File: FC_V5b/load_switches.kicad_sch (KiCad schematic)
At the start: 39 parts, among them U19 AP22652, U21 AP22652, U22 AP22652, U23 AP22652, U24 AP22652, U25 TPS2HB50AQPWPRQ1, U29 AP22652, U6 TPS4H160AQPWPRQ1

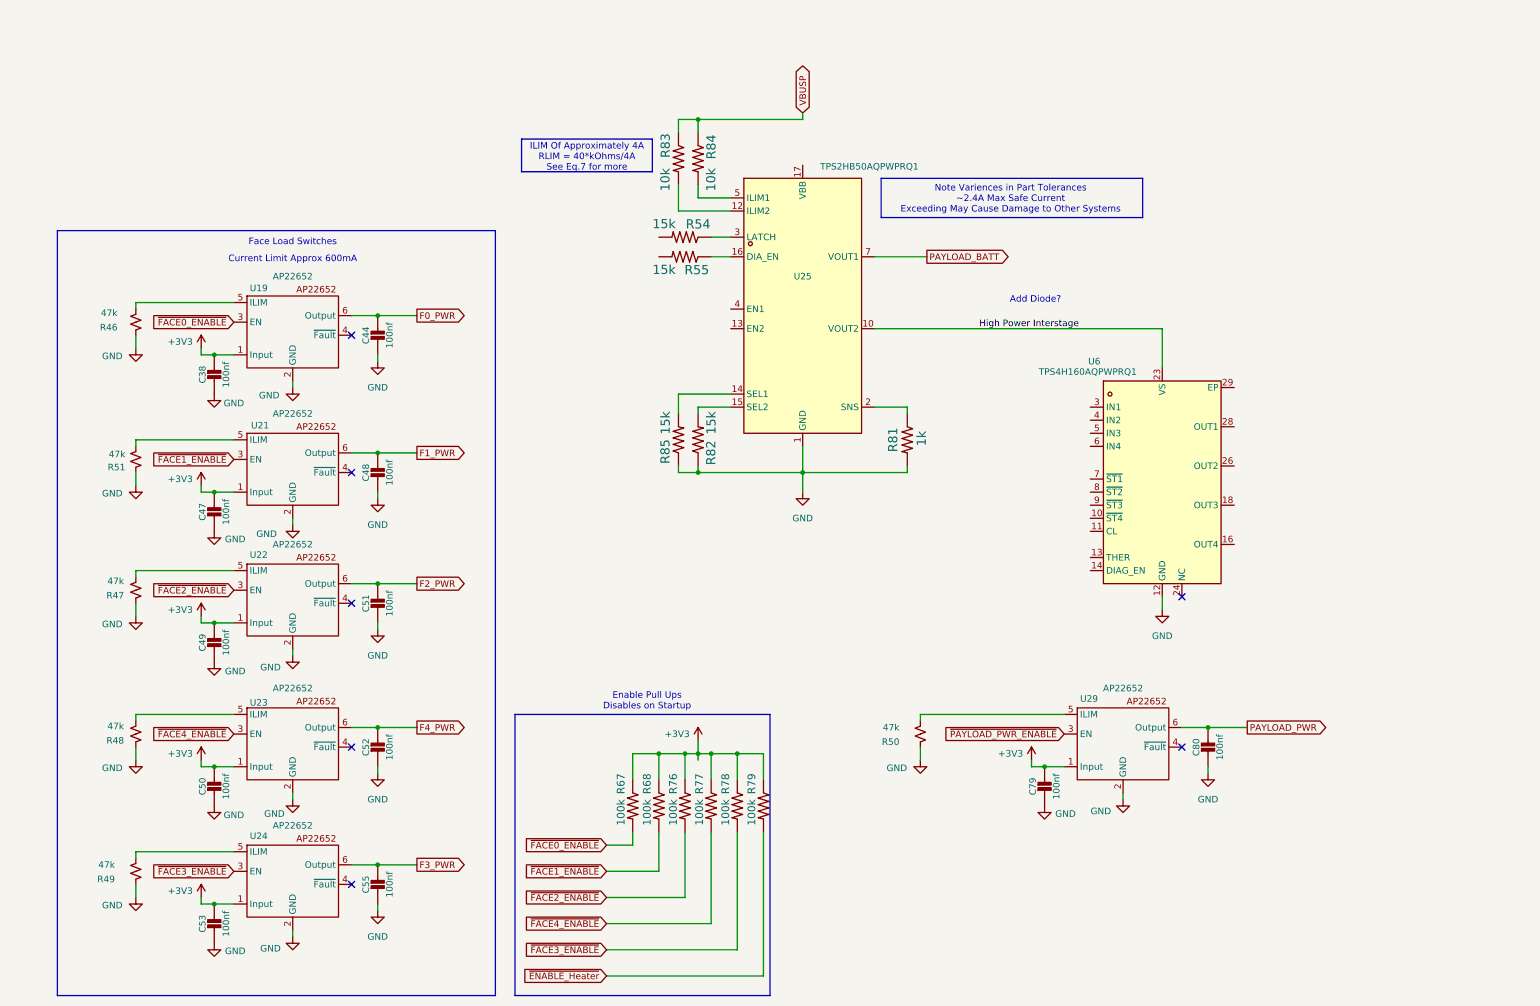
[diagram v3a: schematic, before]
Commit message: Added TPS2 and TPS4 Load Switch Schematics
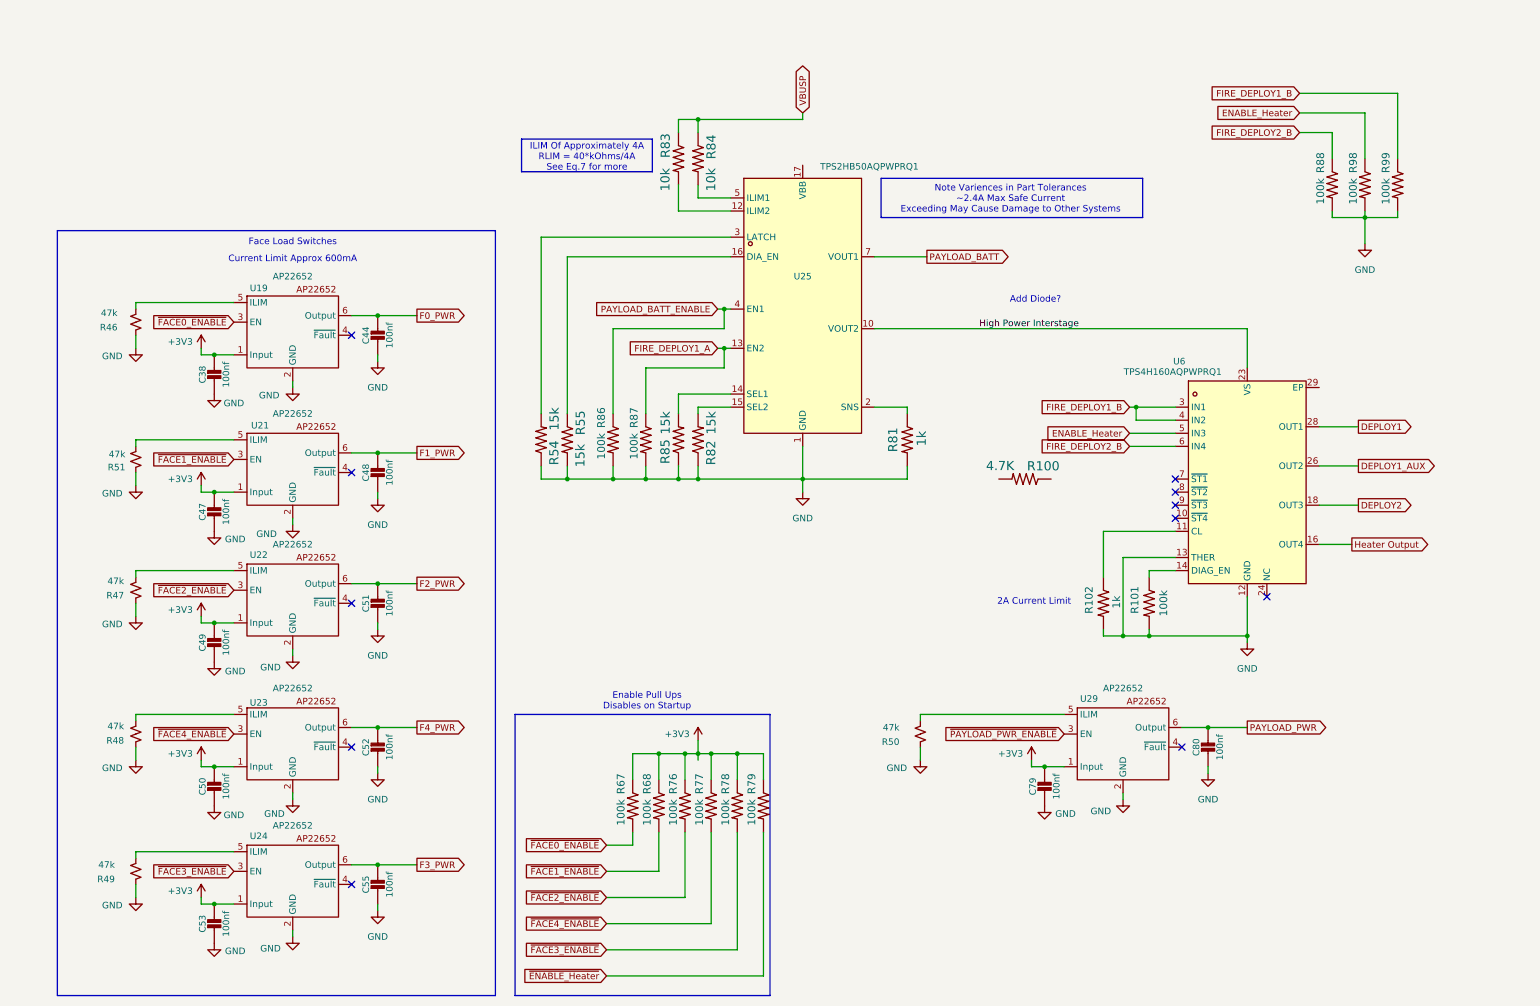
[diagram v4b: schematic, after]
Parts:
- added R100: 4.7K, Resistor_SMD:R_0603_1608Metric, symbol mainboard:RESISTOR0603
- added R101, R86, R87, R88, R98, R99: 100k, Resistor_SMD:R_0603_1608Metric, symbol mainboard:R-US_R0603
- added R102: 1k, Resistor_SMD:R_0603_1608Metric, symbol mainboard:R-US_R0603
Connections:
- net GND: now also R54.1, R55.2, U6.13 (THER), R101.2, R102.2, R86.2, R87.2, R88.2, R98.2, R99.2
- net at U25.3 (LATCH): now also R54.2; no longer R54.1
- net FIRE_DEPLOY1_A: now reaches U25.13 (EN2)
- net FIRE_DEPLOY1_A: now also R87.1
- net PAYLOAD_BATT_ENABLE: now reaches U25.4 (EN1)
- net PAYLOAD_BATT_ENABLE: now also R86.1
- net at U6.11 (CL): now also R102.1
- net at U6.14 (DIAG_EN): now also R101.1
- net Heater Output: now reaches U6.15 (OUT4), U6.16 (OUT4)
- net DEPLOY2: now reaches U6.17 (OUT3), U6.18 (OUT3)
- net DEPLOY1_AUX: now reaches U6.25 (OUT2), U6.26 (OUT2)
- net DEPLOY1: now reaches U6.27 (OUT1), U6.28 (OUT1)
- net FIRE_DEPLOY1_B: now reaches U6.3 (IN1)
- net FIRE_DEPLOY1_B: now also U6.4 (IN2), R99.1
- net ENABLE_Heater: now reaches U6.5 (IN3)
- net ENABLE_Heater: now also R98.1
- net FIRE_DEPLOY2_B: now reaches U6.6 (IN4)
- net FIRE_DEPLOY2_B: now also R88.1
- no-connect marks 7 -> 11
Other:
- note added: "2A Current Limit"
- moved on the sheet: R54, R55, U6

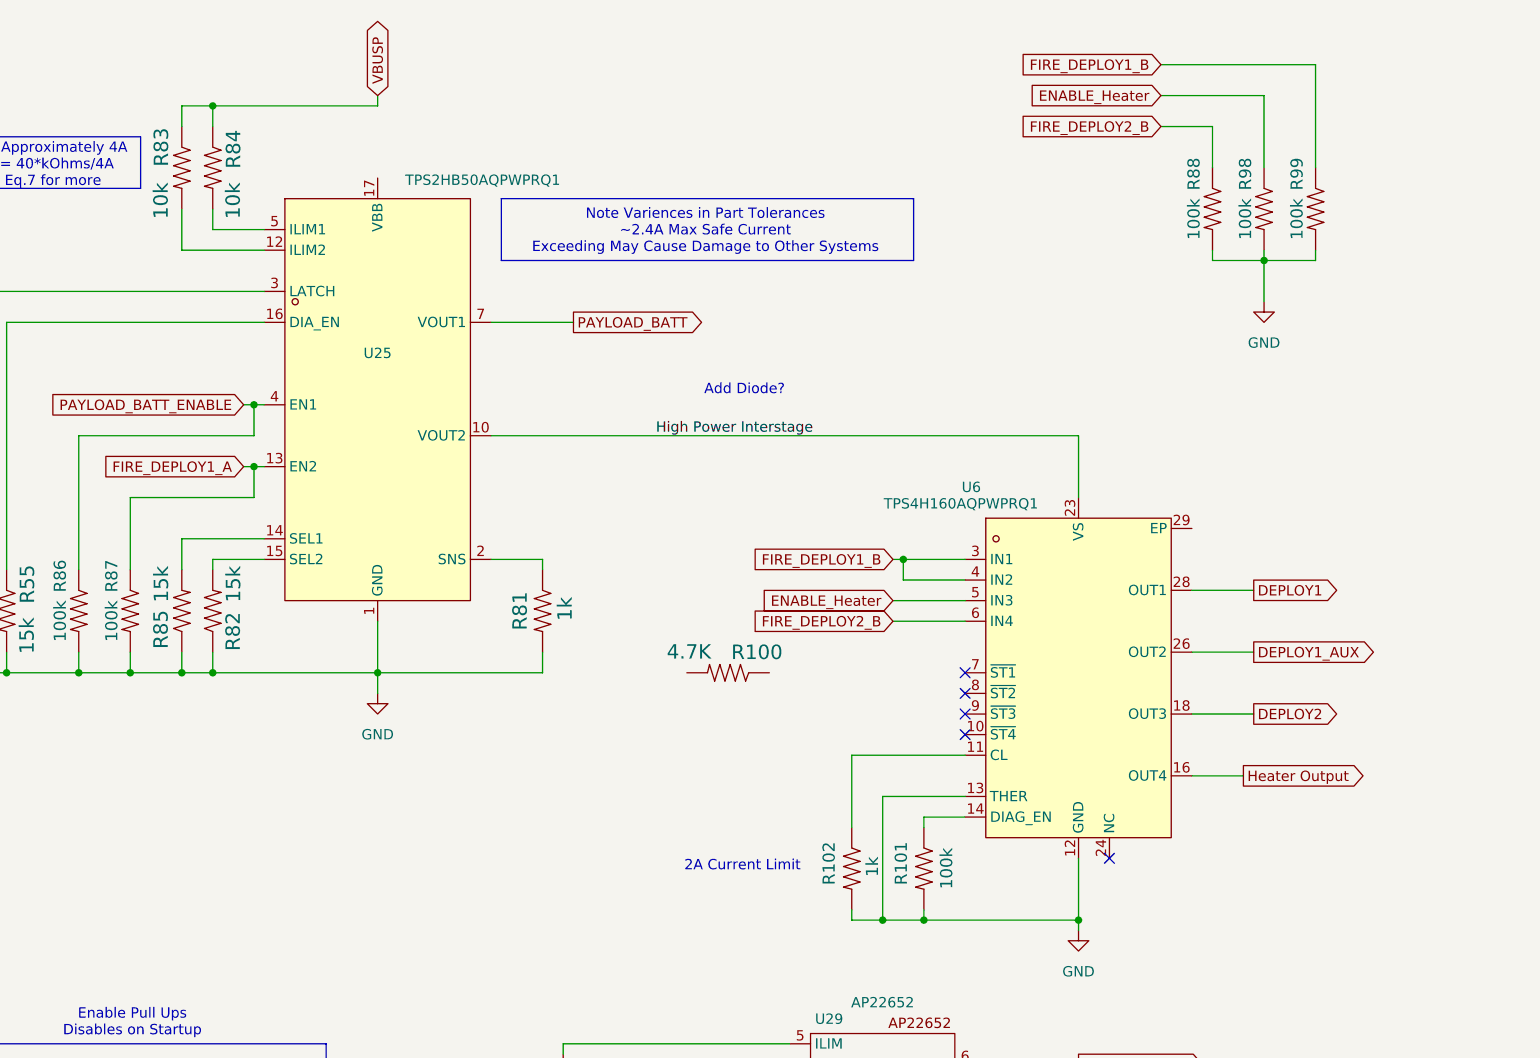
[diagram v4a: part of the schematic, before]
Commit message: Removed Inhibit Bypass Jumper
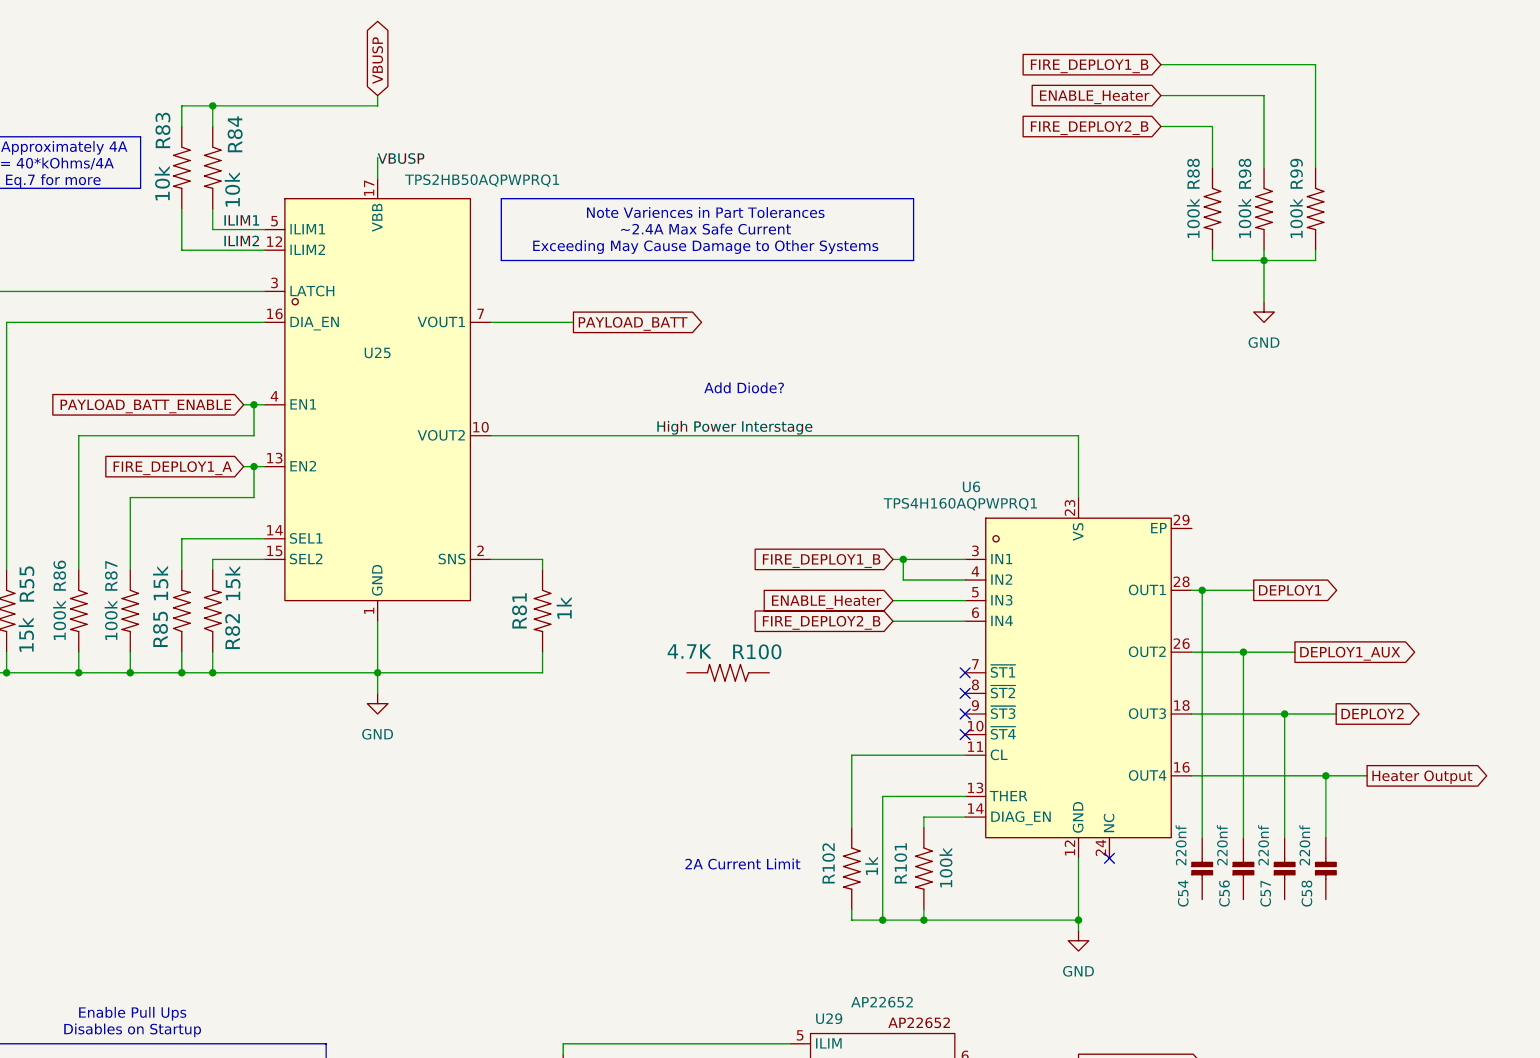
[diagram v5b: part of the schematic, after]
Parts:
- added C54, C56, C57, C58: 220nf, Capacitor_SMD:C_0402_1005Metric, symbol Adafruit ItsyBitsy RP2040-eagle-import:CAP_CERAMIC_0402NO
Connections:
- net DEPLOY1: now also C54.1
- net DEPLOY1_AUX: now also C56.1
- net DEPLOY2: now also C57.1
- net Heater Output: now also C58.1
- net VBUSP: now also U25.17 (VBB)
- net ILIM2: now reaches R83.2, U25.12 (ILIM2)
- net ILIM1: now reaches R84.2, U25.5 (ILIM1)
